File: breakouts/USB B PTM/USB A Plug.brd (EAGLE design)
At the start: 16.1 x 18.1 mm, 7 parts

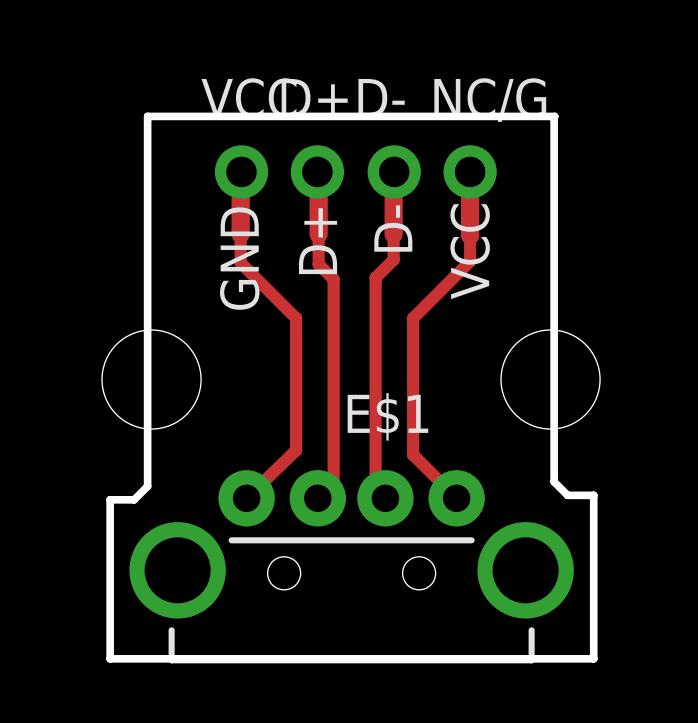
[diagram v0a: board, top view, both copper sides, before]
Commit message: adjusted width of board - hip to be squared
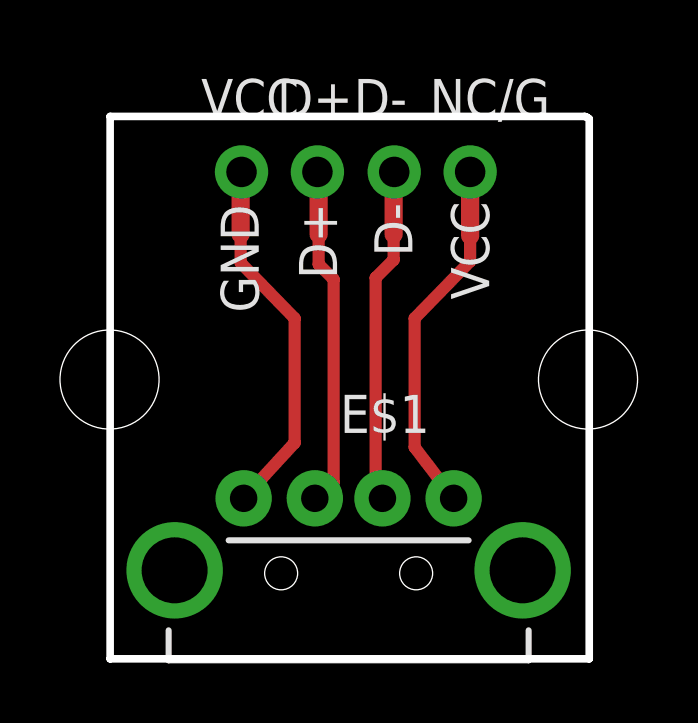
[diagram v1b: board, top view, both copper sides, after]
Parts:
- moved JP4 1.40 mm to (2.78, 25.4)
- moved JP3 1.25 mm to (18.7, 25.4)
- moved E$1 0.10 mm to (10.8, 19.1)
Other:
- board size 16.1 x 18.1 mm -> 16 x 18.1 mm
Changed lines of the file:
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@@
 <board>
 <plain>
-<wire x1="2.8" y1="16.1" x2="2.8" y2="21.4" width="0.254" layer="20"/>
-<wire x1="2.8" y1="21.4" x2="3.6" y2="21.4" width="0.254" layer="20"/>
-<wire x1="3.6" y1="21.4" x2="4.05" y2="21.85" width="0.254" layer="20"/>
-<wire x1="4.05" y1="21.85" x2="4.05" y2="34.18" width="0.254" layer="20"/>
-<wire x1="4.05" y1="34.18" x2="17.62" y2="34.18" width="0.254" layer="20"/>
-<wire x1="17.62" y1="34.18" x2="17.6" y2="34.15" width="0.254" layer="20"/>
-<wire x1="17.6" y1="34.15" x2="17.6" y2="22" width="0.254" layer="20"/>
-<wire x1="17.6" y1="22" x2="18.05" y2="21.55" width="0.254" layer="20"/>
-<wire x1="18.05" y1="21.55" x2="18.92" y2="21.55" width="0.254" layer="20"/>
-<wire x1="18.92" y1="21.55" x2="18.92" y2="16.1" width="0.254" layer="20"/>
-<wire x1="18.92" y1="16.1" x2="2.8" y2="16.1" width="0.254" layer="20"/>
+<wire x1="2.8" y1="16.1" x2="2.8" y2="34.18" width="0.254" layer="20"/>
+<wire x1="2.8" y1="34.18" x2="18.62" y2="34.18" width="0.254" layer="20"/>
+<wire x1="18.62" y1="34.18" x2="18.7" y2="34.15" width="0.254" layer="20"/>
+<wire x1="18.7" y1="34.15" x2="18.77" y2="34.1" width="0.254" layer="20"/>
+<wire x1="18.77" y1="34.1" x2="18.77" y2="16.1" width="0.254" layer="20"/>
+<wire x1="18.77" y1="16.1" x2="2.8" y2="16.1" width="0.254" layer="20"/>
 <text x="6.485" y="31.24" size="1.27" layer="121" font="vector" ratio="15" rot="R270">GND</text>
 <text x="9.095" y="31.29" size="1.27" layer="121" font="vector" ratio="15" rot="R270">D+</text>
@@
 </autorouter>
 <elements>
-<element name="JP3" library="SparkFun" package="STAND-OFF" value="STAND-OFF" x="17.48" y="25.41"/>
-<element name="JP4" library="SparkFun" package="STAND-OFF" value="STAND-OFF" x="4.18" y="25.41"/>
+<element name="JP3" library="SparkFun" package="STAND-OFF" value="STAND-OFF" x="18.73" y="25.41"/>
+<element name="JP4" library="SparkFun" package="STAND-OFF" value="STAND-OFF" x="2.78" y="25.41"/>
 <element name="VCC" library="adafruit" package="1X01-CLEANBIG" value="" x="7.18" y="32.33"/>
 <element name="D-" library="adafruit" package="1X01-CLEANBIG" value="" x="12.27" y="32.33"/>
 <element name="D+" library="adafruit" package="1X01-CLEANBIG" value="" x="9.71" y="32.33"/>
 <element name="NC/G" library="adafruit" package="1X01-CLEANBIG" value="" x="14.8" y="32.33"/>
-<element name="E$1" library="SparkFun" package="USB-A-H" value="" x="10.85" y="19.05" rot="R90"/>
+<element name="E$1" library="SparkFun" package="USB-A-H" value="" x="10.75" y="19.05" rot="R90"/>
 </elements>
 <signals>
@@
 <wire x1="14.8" y1="32.33" x2="14.8" y2="30.2" width="0.6096" layer="1"/>
 <wire x1="14.8" y1="30.2" x2="14.8" y2="29.35" width="0.4064" layer="1"/>
-<wire x1="14.8" y1="29.35" x2="12.9" y2="27.45" width="0.4064" layer="1"/>
-<wire x1="12.9" y1="27.45" x2="12.9" y2="22.9" width="0.4064" layer="1"/>
-<wire x1="12.9" y1="22.9" x2="14.35" y2="21.45" width="0.4064" layer="1"/>
+<wire x1="14.8" y1="29.35" x2="12.95" y2="27.45" width="0.4064" layer="1"/>
+<wire x1="12.95" y1="27.45" x2="12.95" y2="23.15" width="0.4064" layer="1"/>
+<wire x1="12.95" y1="23.15" x2="14.25" y2="21.45" width="0.4064" layer="1"/>
 </signal>
 <signal name="S$2">
@@
 <wire x1="12.25" y1="29.4" x2="11.65" y2="28.8" width="0.4064" layer="1"/>
 <wire x1="11.65" y1="28.8" x2="11.65" y2="21.877" width="0.4064" layer="1"/>
-<wire x1="11.65" y1="21.877" x2="11.977" y2="21.45" width="0.4064" layer="1"/>
+<wire x1="11.65" y1="21.877" x2="11.877" y2="21.45" width="0.4064" layer="1"/>
 </signal>
 <signal name="S$3">
@@
 <wire x1="9.75" y1="29.25" x2="10.25" y2="28.75" width="0.4064" layer="1"/>
 <wire x1="10.25" y1="28.75" x2="10.25" y2="21.977" width="0.4064" layer="1"/>
-<wire x1="10.25" y1="21.977" x2="9.723" y2="21.45" width="0.4064" layer="1"/>
+<wire x1="10.25" y1="21.977" x2="9.623" y2="21.45" width="0.4064" layer="1"/>
 </signal>
 <signal name="S$4">
@@
 <wire x1="7.15" y1="32.33" x2="7.15" y2="30.25" width="0.6096" layer="1"/>
 <wire x1="7.15" y1="30.25" x2="7.15" y2="29.3" width="0.4064" layer="1"/>
-<wire x1="7.15" y1="29.3" x2="9" y2="27.45" width="0.4064" layer="1"/>
-<wire x1="9" y1="27.45" x2="9" y2="23.05" width="0.4064" layer="1"/>
-<wire x1="9" y1="23.05" x2="7.35" y2="21.45" width="0.4064" layer="1"/>
+<wire x1="7.15" y1="29.3" x2="8.95" y2="27.45" width="0.4064" layer="1"/>
+<wire x1="8.95" y1="27.45" x2="8.95" y2="23.3" width="0.4064" layer="1"/>
+<wire x1="8.95" y1="23.3" x2="7.25" y2="21.45" width="0.4064" layer="1"/>
 </signal>
 </signals>
